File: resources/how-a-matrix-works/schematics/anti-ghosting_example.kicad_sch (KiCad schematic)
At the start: 16 parts

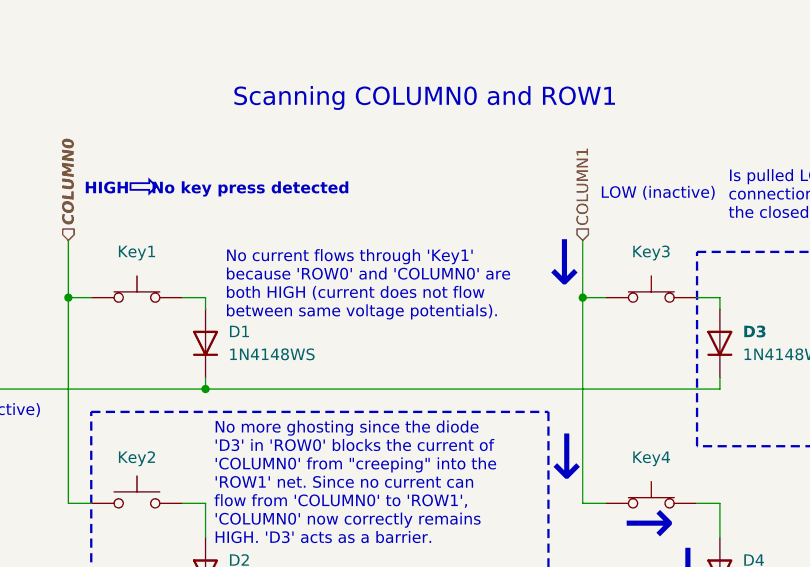
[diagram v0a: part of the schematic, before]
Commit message: fix schematic annotations and order and update images
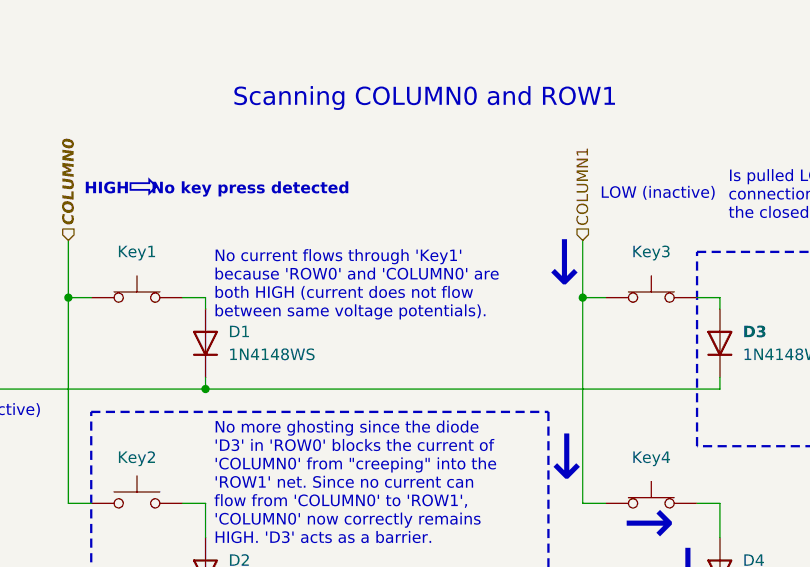
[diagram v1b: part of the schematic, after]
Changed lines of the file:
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@@
 	(text_box "No current flows through 'Key1' because 'ROW0' and 'COLUMN0' are both HIGH (current does not flow between same voltage potentials)."
 		(exclude_from_sim no)
-		(at 74.93 113.03 0)
+		(at 73.66 113.03 0)
 		(size 36.83 8.89)
 		(margins 0.9525 0.9525 0.9525 0.9525)
